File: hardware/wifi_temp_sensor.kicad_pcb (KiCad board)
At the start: 2 copper layers, 50.8 x 45.7 mm, 12 parts, among them J1 USB_B_Mini, J2 ESP8266, J3 TempSensor, J4 Prog, J5 Display, SW1 BootMode, U2 AZ1117-3.3

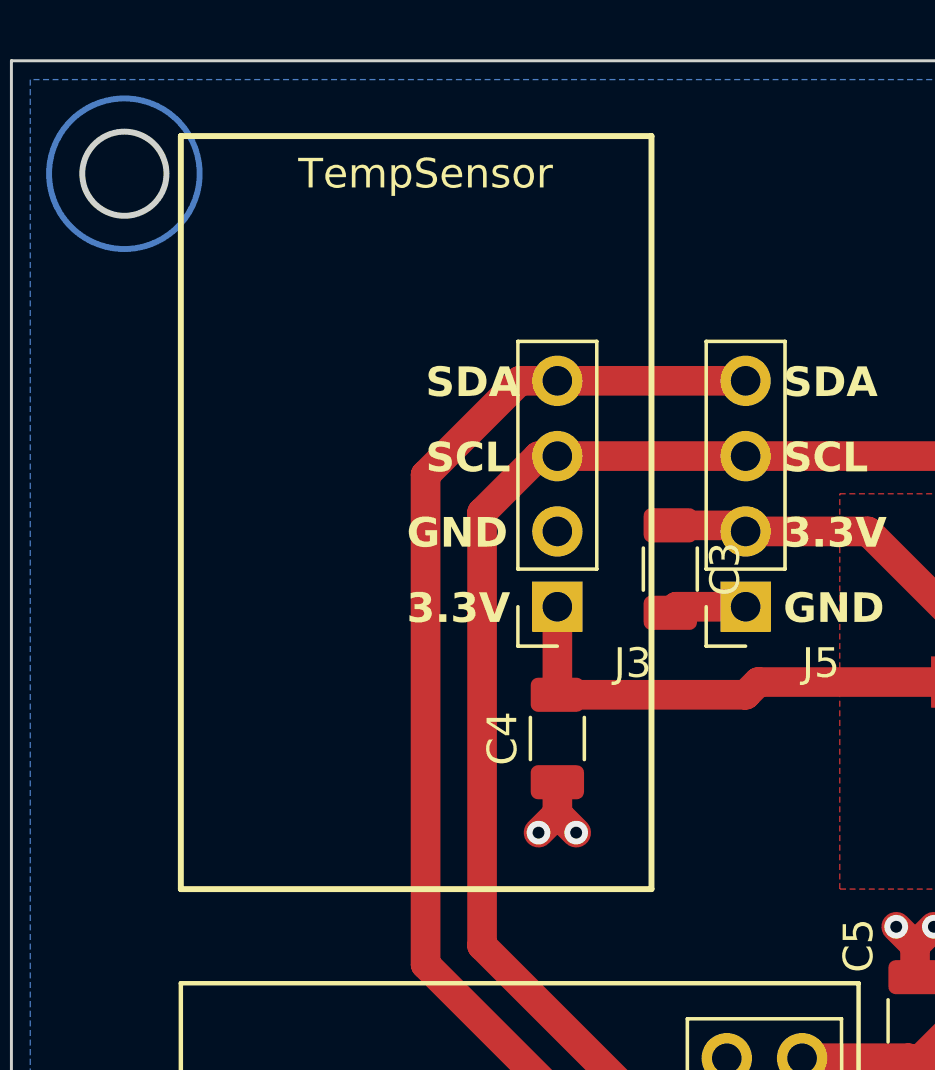
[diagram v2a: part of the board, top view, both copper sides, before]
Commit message: fixed up small warnings on DRC, want to put in right angle switch
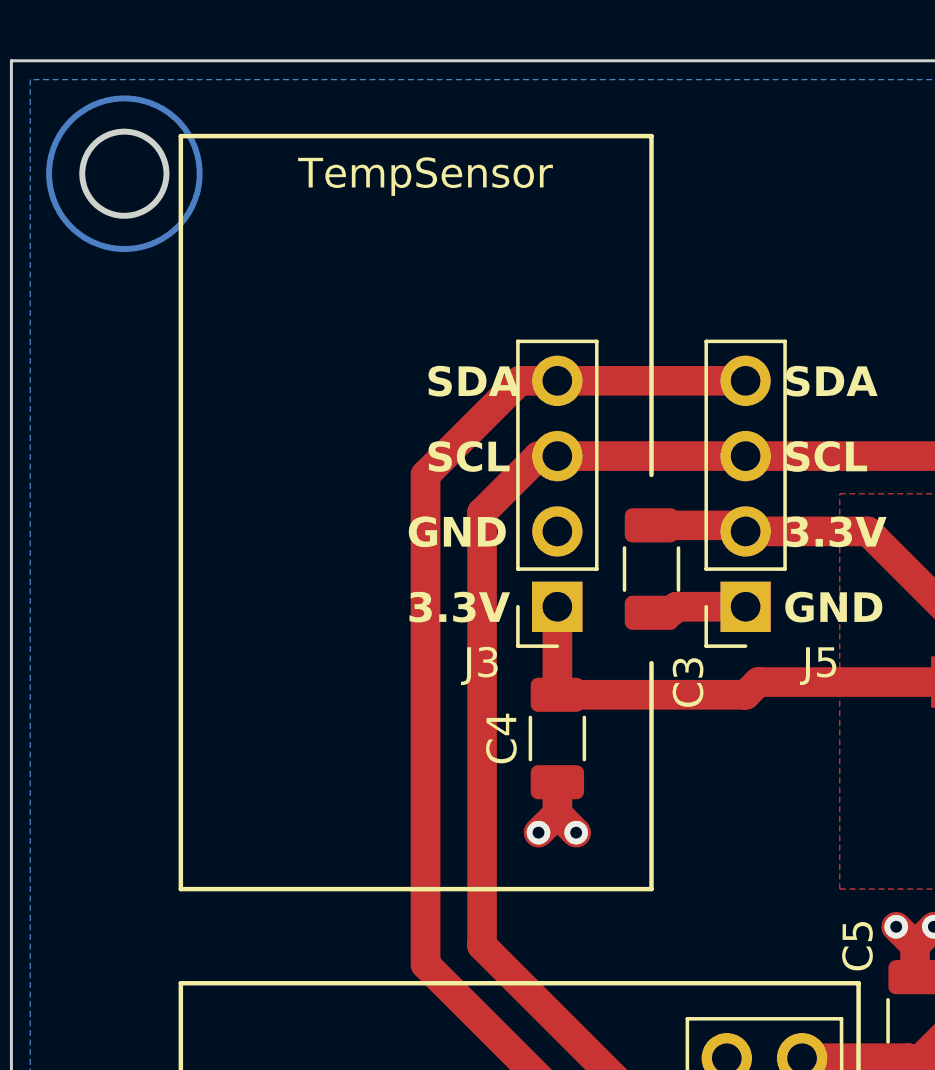
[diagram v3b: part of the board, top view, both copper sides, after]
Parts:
- moved C3 0.64 mm to (205.1, 41.9)
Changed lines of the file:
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@@
   )
   (footprint "Capacitor_SMD:C_1206_3216Metric" (layer "F.Cu")
-    (at 205.74 41.91 -90)
+    (at 205.105 41.91 -90)
     (descr "Capacitor SMD 1206 (3216 Metric), square (rectangular) end terminal, IPC_7351 nominal, (Body size source: IPC-SM-782 page 76, https://www.pcb-3d.com/wordpress/wp-content/uploads/ipc-sm-782a_amendment_1_and_2.pdf), generated with kicad-footprint-generator")
     (tags "capacitor")
@@
     (property "ki_keywords" "capacitor cap")
     (attr smd)
-    (fp_text reference "C3" (at 0 -1.85 90) (layer "F.SilkS")
+    (fp_text reference "C3" (at 3.81 -1.27 90) (layer "F.SilkS")
         (effects (font (size 1 1) (thickness 0.15)))
     )
@@
     (property "ki_keywords" "connector")
     (attr through_hole)
-    (fp_text reference "J3" (at -2.54 -1.905) (layer "F.SilkS")
+    (fp_text reference "J3" (at 2.54 -1.905) (layer "F.SilkS")
         (effects (font (size 1 1) (thickness 0.15)))
     )
@@
   (gr_circle (center 187.325 28.575) (end 189.865 28.575)
     (stroke (width 0.2) (type default)) (fill none) (layer "B.Cu"))
-  (gr_rect (start 189.23 27.305) (end 205.105 52.705)
-    (stroke (width 0.2) (type default)) (fill none) (layer "F.SilkS"))
+  (gr_line (start 205.105 52.705) (end 205.105 45.085)
+    (stroke (width 0.15) (type default)) (layer "F.SilkS"))
+  (gr_line (start 205.105 27.305) (end 189.23 27.305)
+    (stroke (width 0.15) (type default)) (layer "F.SilkS"))
+  (gr_line (start 189.23 27.305) (end 189.23 52.705)
+    (stroke (width 0.15) (type default)) (layer "F.SilkS"))
   (gr_rect (start 220.345 52.705) (end 233.68 69.85)
     (stroke (width 0.15) (type default)) (fill none) (layer "F.SilkS"))
   (gr_rect (start 189.23 55.88) (end 212.09 68.58)
     (stroke (width 0.15) (type default)) (fill none) (layer "F.SilkS"))
+  (gr_line (start 189.23 52.705) (end 205.105 52.705)
+    (stroke (width 0.15) (type default)) (layer "F.SilkS"))
+  (gr_line (start 205.105 27.305) (end 205.105 38.735)
+    (stroke (width 0.15) (type default)) (layer "F.SilkS"))
   (gr_line (start 234.315 47.9425) (end 234.315 24.765)
     (stroke (width 0.1) (type default)) (layer "Edge.Cuts"))

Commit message: Minor tweaks
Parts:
- J4: footprint Connector_PinHeader_2.54mm:PinHeader_1x06_P2.54mm_Vertical -> Connector_PinSocket_2.54mm:PinSocket_1x06_P2.54mm_Horizontal; moved to B.Cu
- moved SW1 1.32 mm to (232.2, 38.0)
- moved C4 1.10 mm to (201.9, 48.7)
- moved C3 0.17 mm to (205.2, 42.0)
- turned J4 to 180 degrees
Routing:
- net +3.3V: track 66.6 -> 68.9 mm
- net SCL: track 58.5 -> 59.2 mm
- net GND: track 29.7 -> 30.3 mm
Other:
- outline, holes or cut-outs redrawn

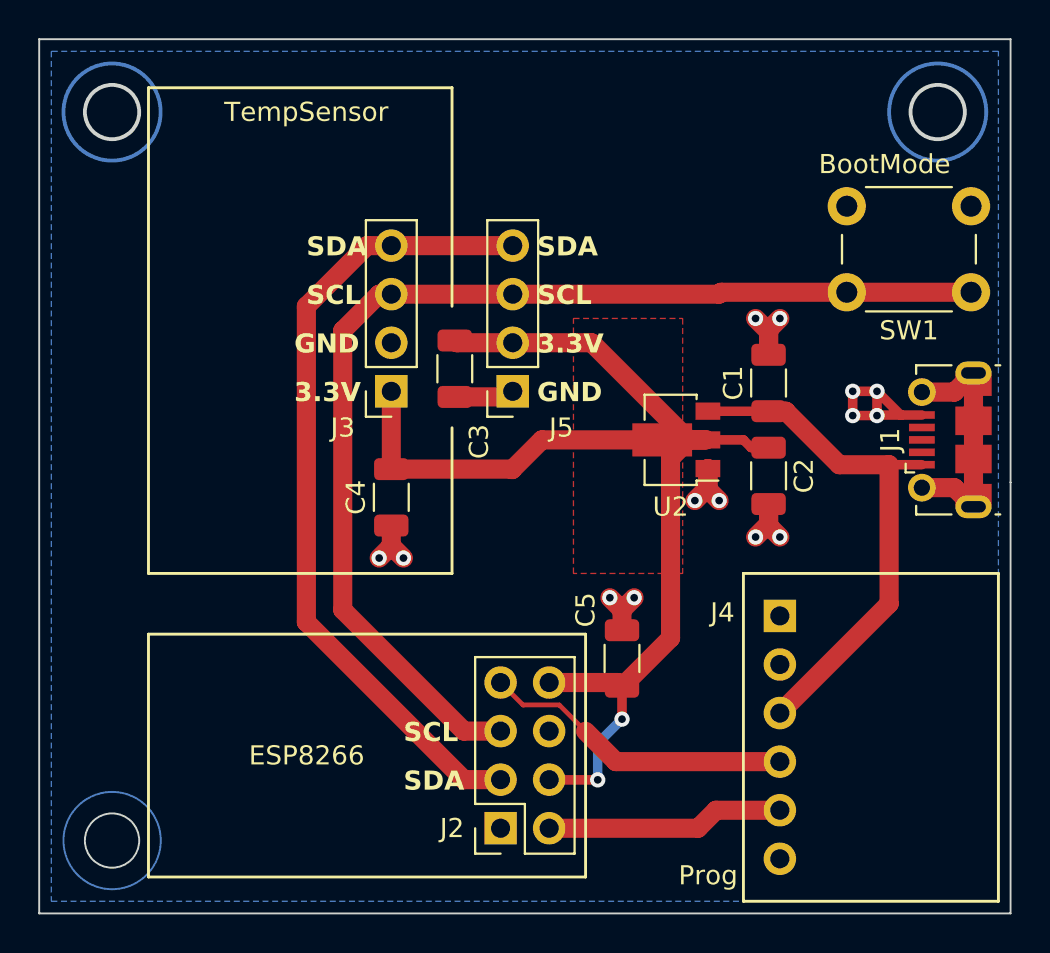
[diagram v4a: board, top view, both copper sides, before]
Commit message: Final mods for V0.3, added right angle switch
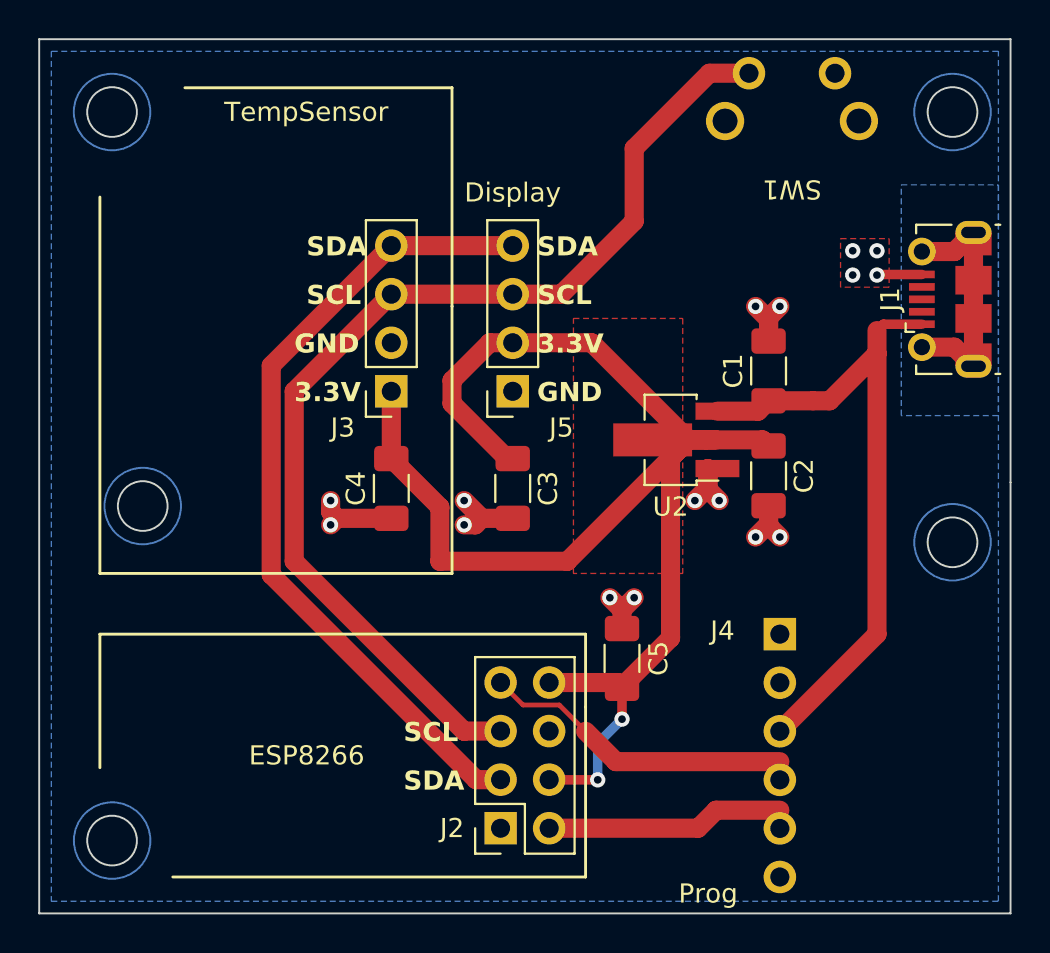
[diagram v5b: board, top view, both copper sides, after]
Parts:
- C1, C2, C3, C4, C5: footprint Capacitor_SMD:C_1206_3216Metric -> Capacitor_SMD:C_1206_3216Metric_Pad1.33x1.80mm_HandSolder
- SW1: footprint Button_Switch_THT:SW_PUSH_6mm -> buttons:TL1105RA
- U2: footprint Package_TO_SOT_SMD:SOT-89-3 -> Package_TO_SOT_SMD:SOT-89-3_Handsoldering
- moved SW1 17.2 mm to (222.9, 23.5)
- moved J1 7.35 mm to (231.1, 38.4)
- moved C3 6.95 mm to (208.3, 48.3)
- moved J4 0.95 mm to (222.2, 55.9)
- moved C1 0.63 mm to (221.7, 42.1)
- moved C4 0.47 mm to (201.9, 48.3)
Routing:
- net +3.3V: track 68.9 -> 81.2 mm
- net +5V: track 27.7 -> 35.1 mm
- net GND: track 30.3 -> 26.2 mm, vias 14 -> 16
- net SCL: track 59.2 -> 56.3 mm
- added copper zone on F.Cu, net GND
- added copper zone on B.Cu, net unconnected-(J1-Shield-Pad6)
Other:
- outline, holes or cut-outs redrawn
- board text added: "WiFi Temp Sensor V0_3 Rich Clubb https://github.com/ richClubb/wifi_temp_sensor"
- board text removed: "WiFi Temp Sensor V0_3 Rich Clubb https://github.com/richClubb/wifi_temp_sensor"
